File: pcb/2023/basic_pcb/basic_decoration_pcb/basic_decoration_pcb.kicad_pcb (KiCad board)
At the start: 2 copper layers, 16 parts, among them J3 Screw_Terminal_01x03, Q1 2N2219

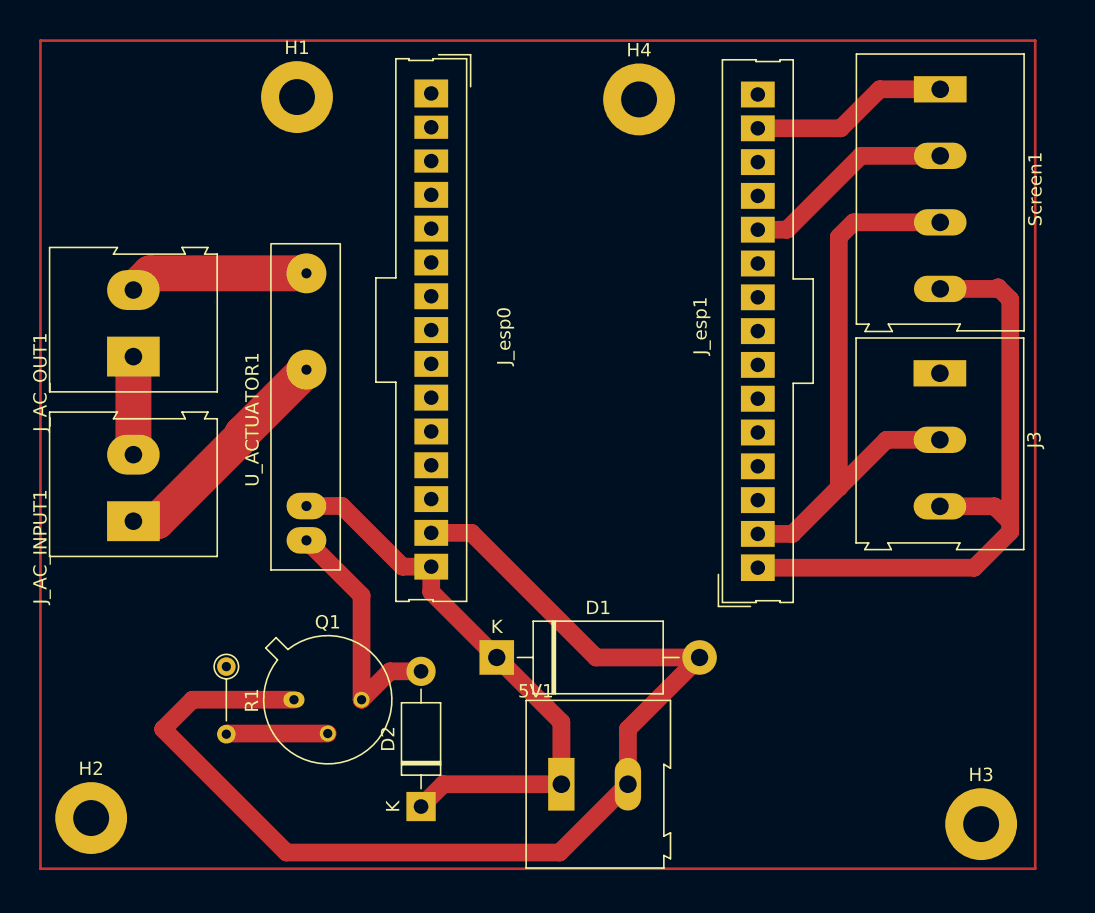
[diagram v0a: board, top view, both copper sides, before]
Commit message: add, added custom solid state relay to the PCB by using optocouplers and triacs, also added the MOC3041 footprint to the esp32 library to keep it within our common resources
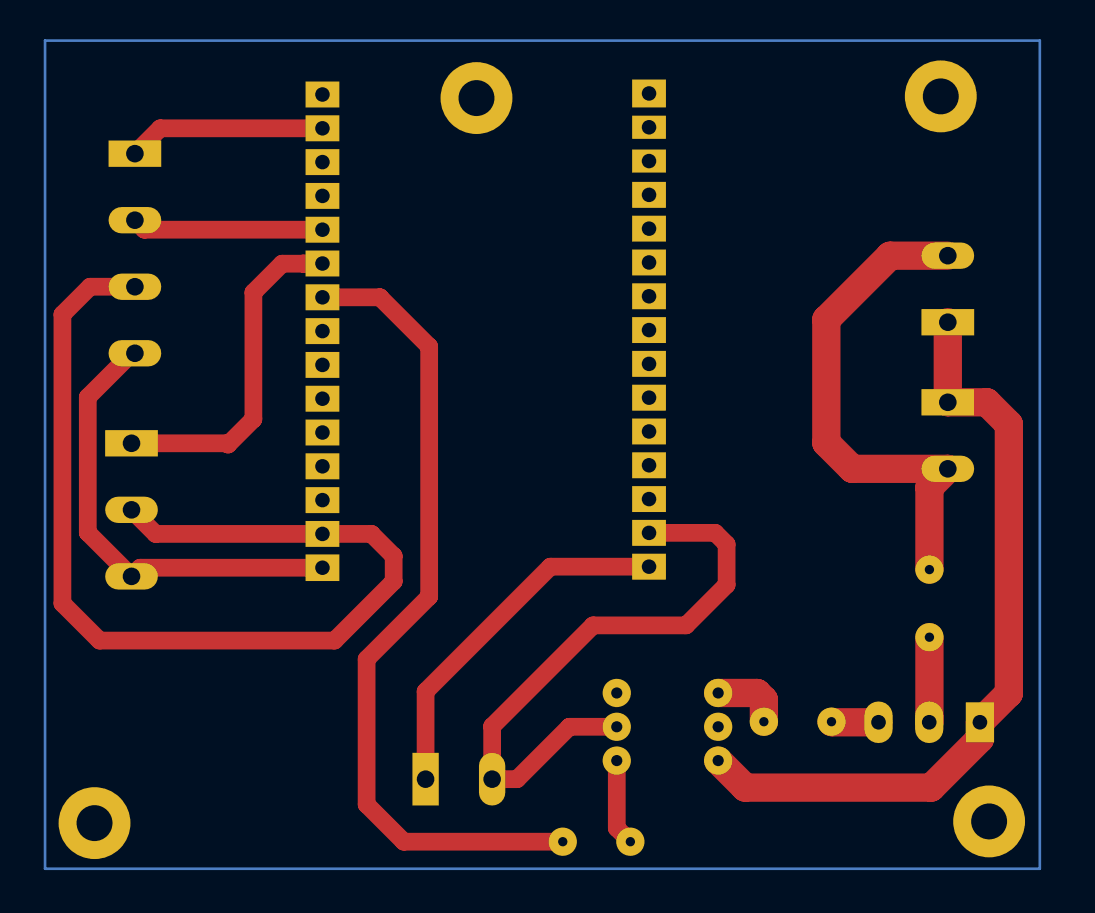
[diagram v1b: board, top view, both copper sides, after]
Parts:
- removed D1: 1N53xxB, Diode_THT:D_DO-201_P15.24mm_Horizontal
- removed D2: 1N4004, Diode_THT:D_DO-41_SOD81_P10.16mm_Horizontal
- removed U_ACTUATOR1: G3MB-202P, smart_sensor:G3MB-202P
- added R2: 470, Resistor_THT:R_Axial_DIN0204_L3.6mm_D1.6mm_P5.08mm_Vertical, B.Cu at (205.5, 100.1)
- added R3: 500, Resistor_THT:R_Axial_DIN0204_L3.6mm_D1.6mm_P5.08mm_Vertical, B.Cu at (217.9, 93.7)
- added U1: MOC3041M, esp32:PDIP6_6P6X8P89_ONS, B.Cu at (194.4, 103.0)
- 5V1, H1, H2, H3, H4, J3, J_AC_INPUT1, J_AC_OUT1, J_esp0, J_esp1, Screen1: moved to B.Cu
- Q1: value 2N2219 -> BT136-500; footprint Package_TO_SOT_THT:TO-39-3 -> Package_TO_SOT_THT:TO-220-3_Vertical; moved to B.Cu
- R1: value 660 -> 470; moved to B.Cu
- moved H2 67.5 mm to (222.4, 107.6), turned to 180 degrees
- moved H3 66.6 mm to (155.2, 107.7), turned to 180 degrees
- moved J_AC_INPUT1 61.8 mm to (219.3, 76.1), turned to -90 degrees
- moved J_AC_OUT1 61.3 mm to (219.3, 70.1)
- moved J3 61.0 mm to (158.0, 79.2)
- moved Screen1 60.7 mm to (158.2, 57.4)
- moved Q1 50.3 mm to (220.5, 100.1), turned to 180 degrees
- moved H1 48.4 mm to (218.8, 53.1), turned to 180 degrees
- moved R1 28.5 mm to (190.4, 109.1), turned to 0 degrees
- moved J_esp1 16.4 mm to (180.5, 70.3)
- moved H4 12.2 mm to (183.9, 53.2), turned to 180 degrees
- moved 5V1 10.2 mm to (180.1, 104.4)
- moved J_esp0 0.07 mm to (188.7, 71.1)
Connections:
- J3 pad 1: D2 -> D19
- J_AC_INPUT1 pad 1: AC1 -> AC1_IN
- J_AC_INPUT1 pad 2: AC2 -> AC2_IN
- J_AC_OUT1 pad 1: AC2 -> AC1_IN
- J_AC_OUT1 pad 2: Net-(J_AC_OUT1-Pin_2) -> AC2_IN
- Q1 pad 1: GND5V -> AC1_IN
- Q1 pad 2: Net-(Q1-B) -> Net-(Q1-A2)
- R1 pad 1: D22 -> D18
- R1 pad 2: Net-(Q1-B) -> Net-(R1-Pad2)
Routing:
- net D18: track 0.00 -> 61.8 mm
- net AC1_IN: track 0.00 -> 57.9 mm
- net GND5V: track 87.4 -> 46.2 mm
- net AC2_IN: track 0.00 -> 38.5 mm
- net GND2: track 43.5 -> 79.0 mm
- net D19: track 0.00 -> 26.6 mm
- net AC1: track 17.8 -> 0.00 mm
- net 5v: track 42.9 -> 27.3 mm
- net Net-(Q1-G): track 19.0 -> 3.55 mm
- net 3V3: track 49.0 -> 34.3 mm
- net Net-(J_AC_OUT1-Pin_2): track 13.5 -> 0.00 mm
- net Net-(Q1-B): track 7.64 -> 0.00 mm
- net AC2: track 7.37 -> 0.00 mm
- net Net-(R1-Pad2): track 0.00 -> 6.52 mm
- net Net-(Q1-A2): track 0.00 -> 6.40 mm
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
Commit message: update, fixed an error in the PCB and now any AC appliance which get's connected can work
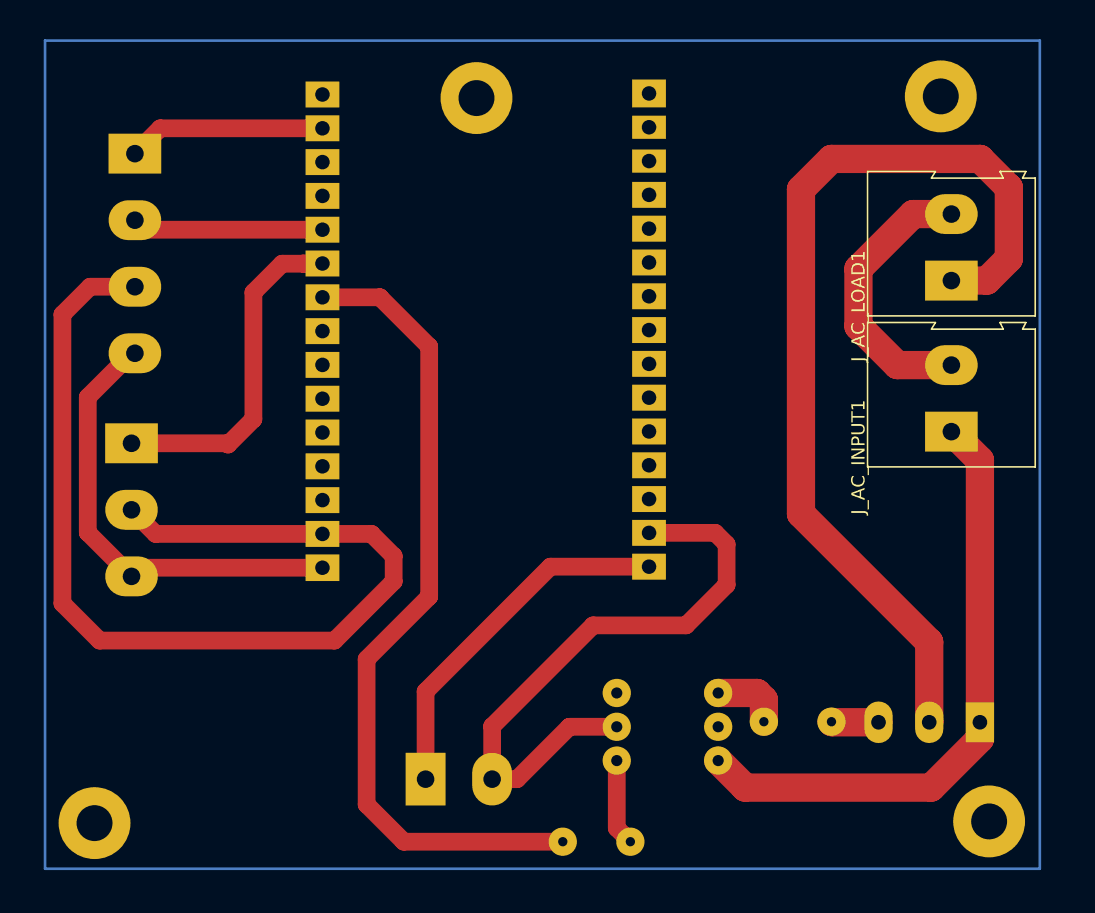
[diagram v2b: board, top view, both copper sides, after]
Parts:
- removed J_AC_OUT1: Screw_Terminal_01x02, TerminalBlock:TerminalBlock_Altech_AK300-2_P5.00mm
- removed R3: 500, Resistor_THT:R_Axial_DIN0204_L3.6mm_D1.6mm_P5.08mm_Vertical
- added J_AC_LOAD1: Screw_Terminal_01x02, TerminalBlock:TerminalBlock_Altech_AK300-2_P5.00mm, F.Cu at (219.6, 66.9)
- J_AC_INPUT1: moved to F.Cu
- moved J_AC_INPUT1 2.22 mm to (219.6, 78.3), turned to 90 degrees
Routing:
- net Net-(J_AC_LOAD1-Pin_1): track 6.40 -> 71.9 mm
- net AC2_IN: track 38.5 -> 21.2 mm
- net AC1_IN: track 57.9 -> 46.0 mm

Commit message: update, fixed bug on the PCB, a wrong connection between the BT136 and the actuators wasn't making it work
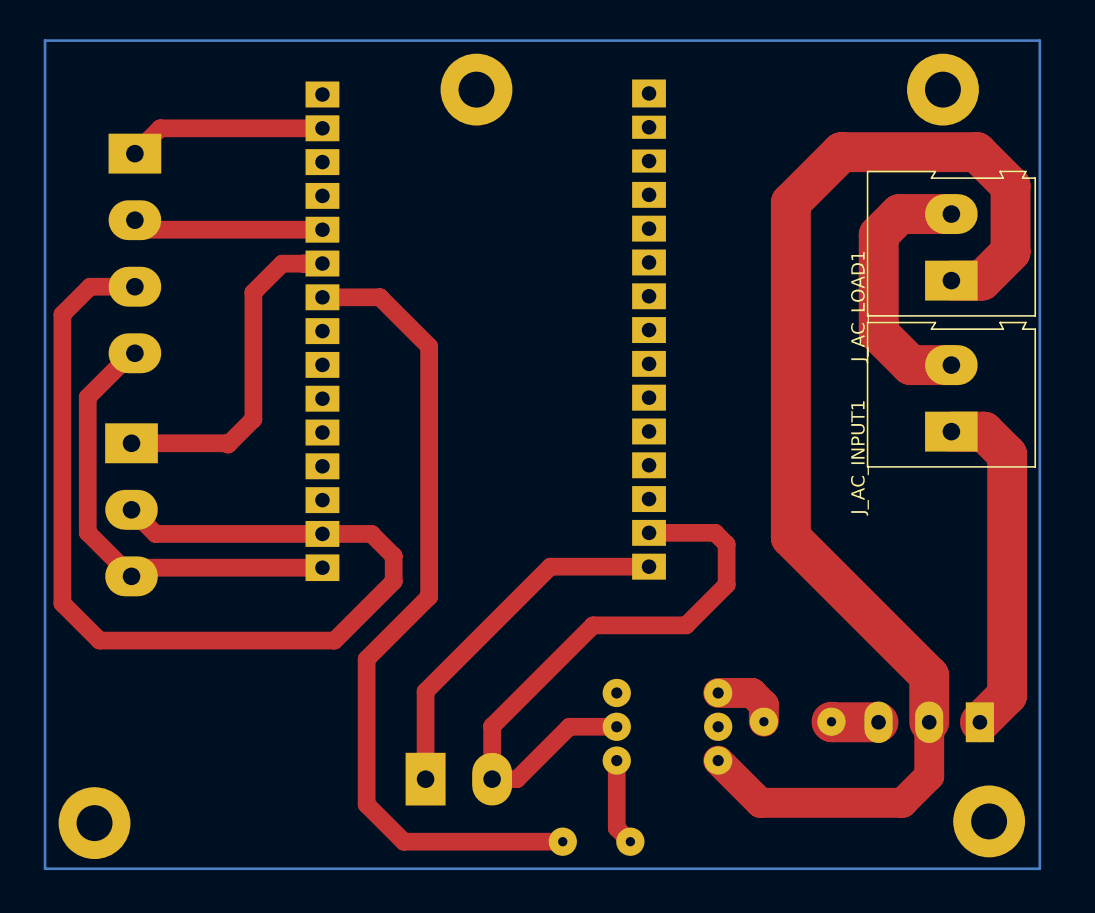
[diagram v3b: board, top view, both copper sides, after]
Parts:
- moved H4 0.63 mm to (183.9, 52.6)
- moved H1 0.53 mm to (218.9, 52.6)
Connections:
- U1 pad 6: AC1_IN -> Net-(J_AC_LOAD1-Pin_1)
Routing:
- net Net-(J_AC_LOAD1-Pin_1): track 71.9 -> 94.8 mm
- net AC1_IN: track 46.0 -> 25.9 mm
- net AC2_IN: track 21.2 -> 19.9 mm
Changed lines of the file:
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@@
   )
   (footprint "MountingHole:MountingHole_2.7mm_M2.5_Pad" (layer "B.Cu")
-    (at 218.78556 53.086 180)
+    (at 218.948 52.578 180)
     (descr "Mounting Hole 2.7mm, M2.5")
     (tags "mounting hole 2.7mm m2.5")
@@
   )
   (footprint "MountingHole:MountingHole_2.7mm_M2.5_Pad" (layer "B.Cu")
-    (at 183.896 53.213 180)
+    (at 183.896 52.578 180)
     (descr "Mounting Hole 2.7mm, M2.5")
     (tags "mounting hole 2.7mm m2.5")
@@
       (net 35 "unconnected-(U1-NC-Pad5)") (pinfunction "NC") (pintype "no_connect"))
     (pad "6" thru_hole circle (at 7.62 0) (size 2.125 2.125) (drill 0.8382) (layers "*.Cu" "*.Mask")
-      (net 36 "AC1_IN") (pintype "passive"))
+      (net 38 "Net-(J_AC_LOAD1-Pin_1)") (pintype "passive"))
   )
   (footprint "Resistor_THT:R_Axial_DIN0204_L3.6mm_D1.6mm_P5.08mm_Vertical" (layer "B.Cu")
@@
   (segment (start 185.071 100.425) (end 192.659 92.837) (width 1.333) (layer "F.Cu") (net 2))
   (segment (start 192.659 92.837) (end 199.644 92.837) (width 1.333) (layer "F.Cu") (net 2))
-  (segment (start 210.6145 100.11825) (end 210.57225 100.076) (width 2.125) (layer "F.Cu") (net 3))
-  (segment (start 214.107 100.11825) (end 210.6145 100.11825) (width 2.125) (layer "F.Cu") (net 3))
+  (segment (start 210.6145 100.11825) (end 210.57225 100.076) (width 3) (layer "F.Cu") (net 3))
+  (segment (start 214.107 100.11825) (end 210.6145 100.11825) (width 3) (layer "F.Cu") (net 3))
   (segment (start 158.227 57.39) (end 160.1322 55.4848) (width 1.333) (layer "F.Cu") (net 4))
   (segment (start 160.1322 55.4848) (end 172.32146 55.4848) (width 1.333) (layer "F.Cu") (net 4))
@@
   (segment (start 194.437 102.997) (end 194.437 108.07075) (width 1.333) (layer "F.Cu") (net 32))
   (segment (start 194.437 108.07075) (end 195.45925 109.093) (width 1.333) (layer "F.Cu") (net 32))
-  (segment (start 204.978 97.917) (end 202.057 97.917) (width 2.125) (layer "F.Cu") (net 33))
-  (segment (start 202.184 98.044) (end 202.057 97.917) (width 1.333) (layer "F.Cu") (net 33))
-  (segment (start 205.49225 100.076) (end 205.49225 98.43125) (width 2.125) (layer "F.Cu") (net 33))
-  (segment (start 205.49225 98.43125) (end 204.978 97.917) (width 2.125) (layer "F.Cu") (net 33))
-  (segment (start 221.727 80.423) (end 219.583 78.279) (width 2.125) (layer "F.Cu") (net 36))
-  (segment (start 202.057 102.997) (end 204.089 105.029) (width 2.125) (layer "F.Cu") (net 36))
-  (segment (start 221.727 101.361) (end 221.727 100.11825) (width 2.125) (layer "F.Cu") (net 36))
-  (segment (start 204.089 105.029) (end 218.059 105.029) (width 2.125) (layer "F.Cu") (net 36))
-  (segment (start 221.727 100.11825) (end 221.727 80.423) (width 2.125) (layer "F.Cu") (net 36))
-  (segment (start 218.059 105.029) (end 221.727 101.361) (width 2.125) (layer "F.Cu") (net 36))
-  (segment (start 212.598 70.358) (end 212.598 66.04) (width 2.125) (layer "F.Cu") (net 37))
-  (segment (start 212.598 66.04) (end 216.709 61.929) (width 2.125) (layer "F.Cu") (net 37))
-  (segment (start 219.583 73.279) (end 215.519 73.279) (width 2.125) (layer "F.Cu") (net 37))
-  (segment (start 215.519 73.279) (end 212.598 70.358) (width 2.125) (layer "F.Cu") (net 37))
-  (segment (start 216.709 61.929) (end 219.583 61.929) (width 2.125) (layer "F.Cu") (net 37))
-  (segment (start 217.932 100.10325) (end 217.917 100.11825) (width 2.125) (layer "F.Cu") (net 38))
-  (segment (start 208.28 84.455) (end 208.28 60.071) (width 2.125) (layer "F.Cu") (net 38))
-  (segment (start 223.901 59.944) (end 223.901 65.278) (width 2.125) (layer "F.Cu") (net 38))
-  (segment (start 222.25 66.929) (end 219.583 66.929) (width 2.125) (layer "F.Cu") (net 38))
-  (segment (start 208.28 60.071) (end 210.566 57.785) (width 2.125) (layer "F.Cu") (net 38))
-  (segment (start 217.917 100.11825) (end 217.917 94.092) (width 2.125) (layer "F.Cu") (net 38))
-  (segment (start 217.917 94.092) (end 208.28 84.455) (width 2.125) (layer "F.Cu") (net 38))
-  (segment (start 223.901 65.278) (end 222.25 66.929) (width 2.125) (layer "F.Cu") (net 38))
-  (segment (start 221.742 57.785) (end 223.901 59.944) (width 2.125) (layer "F.Cu") (net 38))
-  (segment (start 210.566 57.785) (end 221.742 57.785) (width 2.125) (layer "F.Cu") (net 38))
+  (segment (start 205.49225 98.81225) (end 205.49225 100.076) (width 2.25) (layer "F.Cu") (net 33))
+  (segment (start 202.057 97.917) (end 204.597 97.917) (width 2.25) (layer "F.Cu") (net 33))
+  (segment (start 204.597 97.917) (end 205.49225 98.81225) (width 2.25) (layer "F.Cu") (net 33))
+  (segment (start 223.774 98.07125) (end 221.727 100.11825) (width 3) (layer "F.Cu") (net 36))
+  (segment (start 219.583 78.279) (end 222.043 78.279) (width 3) (layer "F.Cu") (net 36))
+  (segment (start 222.043 78.279) (end 223.774 80.01) (width 3) (layer "F.Cu") (net 36))
+  (segment (start 223.774 80.01) (end 223.774 98.07125) (width 3) (layer "F.Cu") (net 36))
+  (segment (start 219.583 73.279) (end 216.535 73.279) (width 3) (layer "F.Cu") (net 37))
+  (segment (start 214.122 63.5) (end 215.693 61.929) (width 3) (layer "F.Cu") (net 37))
+  (segment (start 214.122 70.866) (end 214.122 63.5) (width 3) (layer "F.Cu") (net 37))
+  (segment (start 215.693 61.929) (end 219.583 61.929) (width 3) (layer "F.Cu") (net 37))
+  (segment (start 216.535 73.279) (end 214.122 70.866) (width 3) (layer "F.Cu") (net 37))
+  (segment (start 217.917 100.11825) (end 217.917 96.632) (width 3) (layer "F.Cu") (net 38))
+  (segment (start 205.232 106.172) (end 215.9 106.172) (width 2.25) (layer "F.Cu") (net 38))
+  (segment (start 207.518 61.087) (end 211.328 57.277) (width 3) (layer "F.Cu") (net 38))
+  (segment (start 215.9 106.172) (end 217.917 104.155) (width 2.25) (layer "F.Cu") (net 38))
+  (segment (start 202.057 102.997) (end 205.232 106.172) (width 2.25) (layer "F.Cu") (net 38))
+  (segment (start 217.917 96.632) (end 207.518 86.233) (width 3) (layer "F.Cu") (net 38))
+  (segment (start 221.869 66.929) (end 219.583 66.929) (width 3) (layer "F.Cu") (net 38))
+  (segment (start 217.917 104.155) (end 217.917 100.11825) (width 2.25) (layer "F.Cu") (net 38))
+  (segment (start 207.518 86.233) (end 207.518 61.087) (width 3) (layer "F.Cu") (net 38))
+  (segment (start 224.028 59.817) (end 224.028 64.77) (width 3) (layer "F.Cu") (net 38))
+  (segment (start 221.488 57.277) (end 224.028 59.817) (width 3) (layer "F.Cu") (net 38))
+  (segment (start 211.328 57.277) (end 221.488 57.277) (width 3) (layer "F.Cu") (net 38))
+  (segment (start 224.028 64.77) (end 221.869 66.929) (width 3) (layer "F.Cu") (net 38))
   (group "" (id 2a59f142-c27c-400a-b5f5-f0bce66af96a)
     (members

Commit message: update, fixed bug on the PCB, a pull up resistor is required for the DHT11 to work well, so now it's added
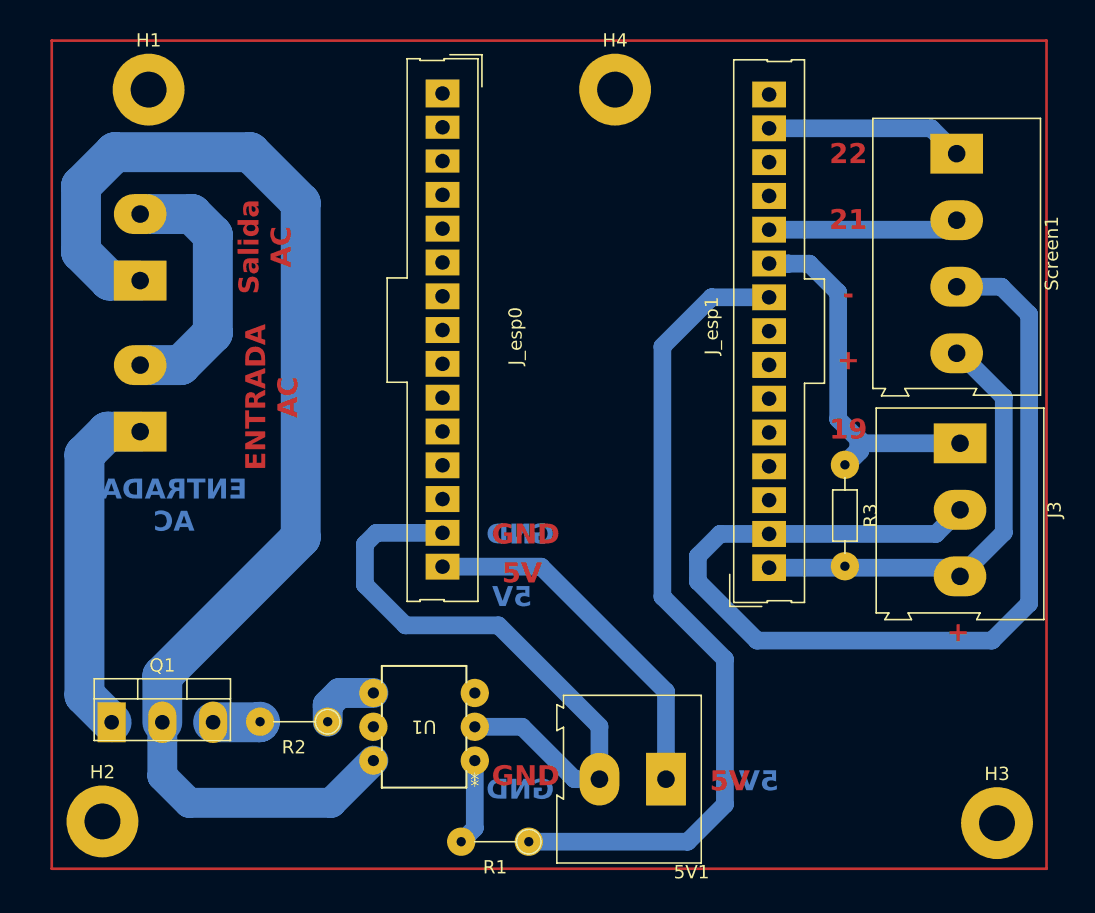
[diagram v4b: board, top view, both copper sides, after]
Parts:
- added R3: 4.7k_0603, Resistor_THT:R_Axial_DIN0204_L3.6mm_D1.6mm_P7.62mm_Horizontal, F.Cu at (211.6, 80.8)
- 5V1, H1, H2, H3, H4, J3, J_esp0, J_esp1, Q1, R1, R2, Screen1, U1: moved to F.Cu
- J_AC_INPUT1, J_AC_LOAD1: moved to B.Cu
- moved H3 67.8 mm to (223.0, 107.7), turned to 0 degrees
- moved H2 66.6 mm to (155.8, 107.6), turned to 0 degrees
- moved Q1 62.7 mm to (157.7, 100.1), turned to 0 degrees
- moved J3 62.3 mm to (220.2, 79.2)
- moved Screen1 61.8 mm to (220.0, 57.4)
- moved J_AC_INPUT1 61.0 mm to (158.6, 78.3)
- moved J_AC_LOAD1 61.0 mm to (158.6, 66.9)
- moved H1 59.7 mm to (159.3, 52.6), turned to 0 degrees
- moved R2 32.8 mm to (172.7, 100.1), turned to 180 degrees
- moved 5V1 18.1 mm to (198.1, 104.4), turned to 180 degrees
- moved J_esp1 17.3 mm to (197.7, 70.3)
- moved U1 10.7 mm to (183.8, 103.0), turned to 180 degrees
- moved H4 10.4 mm to (194.3, 52.6), turned to 0 degrees
- moved R1 2.55 mm to (187.8, 109.1), turned to 180 degrees
- moved J_esp0 0.78 mm to (189.5, 71.1)
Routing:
- net D19: track 26.6 -> 28.9 mm
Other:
- board text added: "+"
- board text added: "-"
- board text added: "19"
- board text added: "21"
- board text added: "22"
- board text added: "5V"
- board text added: "ENTRADA AC"
- board text added: "GND"
- board text added: "Salida AC"
